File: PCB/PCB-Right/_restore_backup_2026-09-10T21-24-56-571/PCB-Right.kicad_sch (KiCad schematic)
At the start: 56 parts, among them J1 USB_C_Receptacle_USB2.0_16P, J2 Conn_ARM_JTAG_SWD_10, Q1 2N7002, SW1 SW_RST, SW2 SW_SPDT, U2 XC6206PxxxMR, U3 SRV05-4, U4 BQ24075RGT, U5 MDBT50Q-1MV2, Y1 32.768KHz

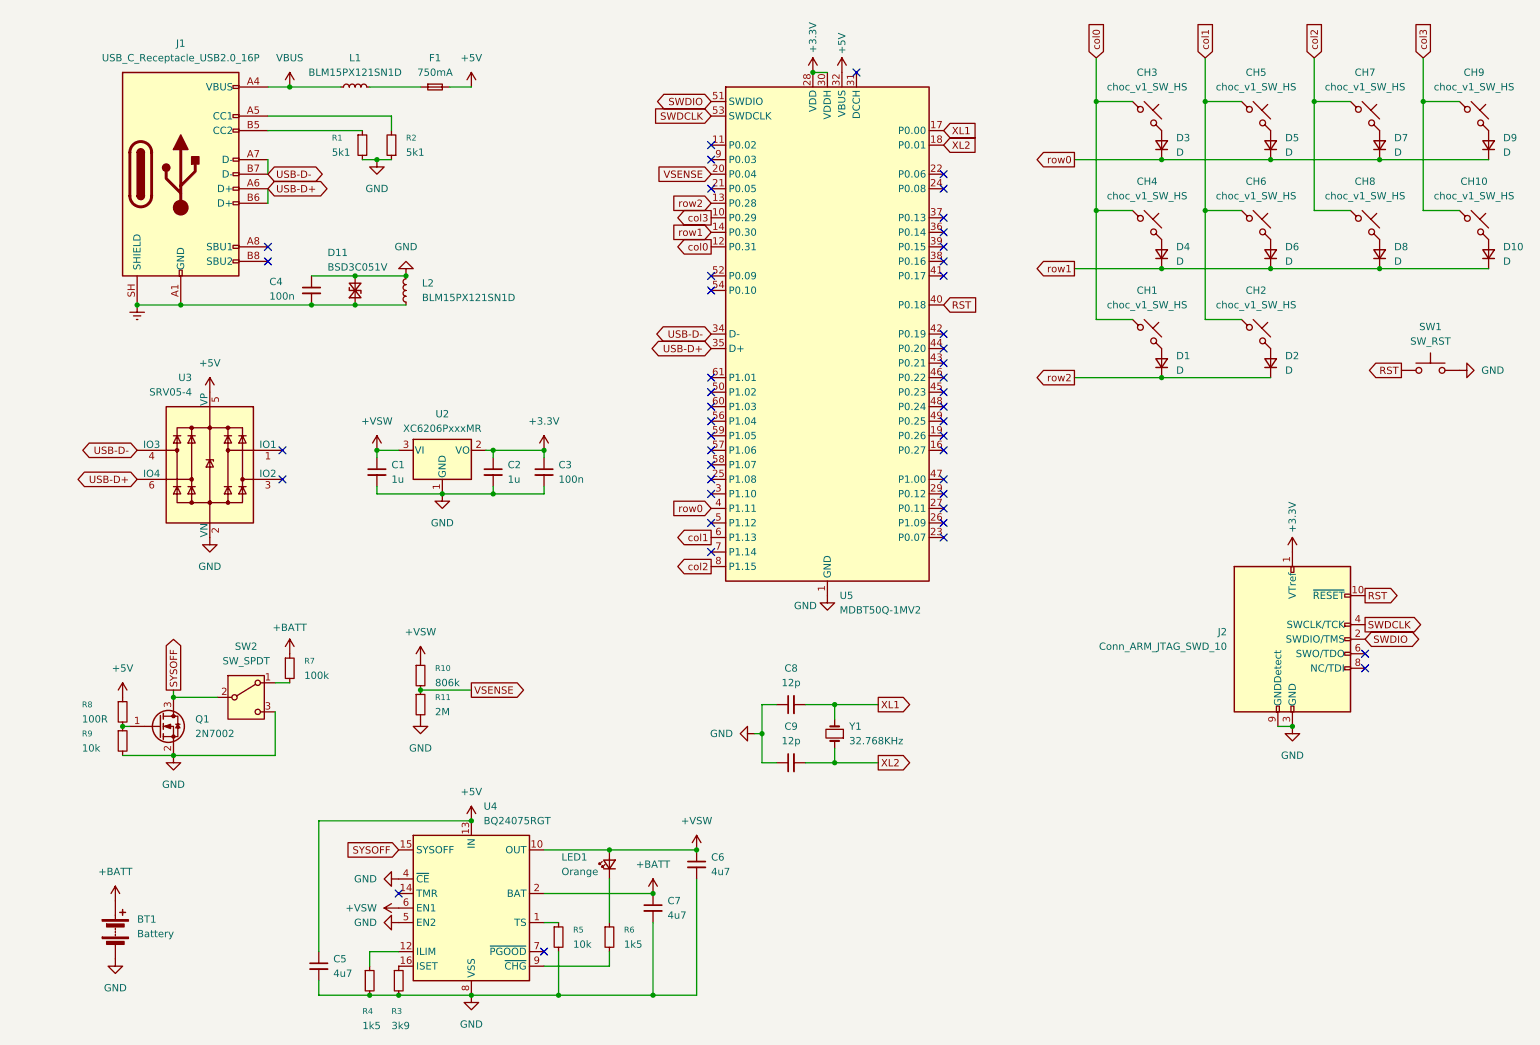
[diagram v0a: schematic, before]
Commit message: PCB Right
Switched to raytac module
gasket mount
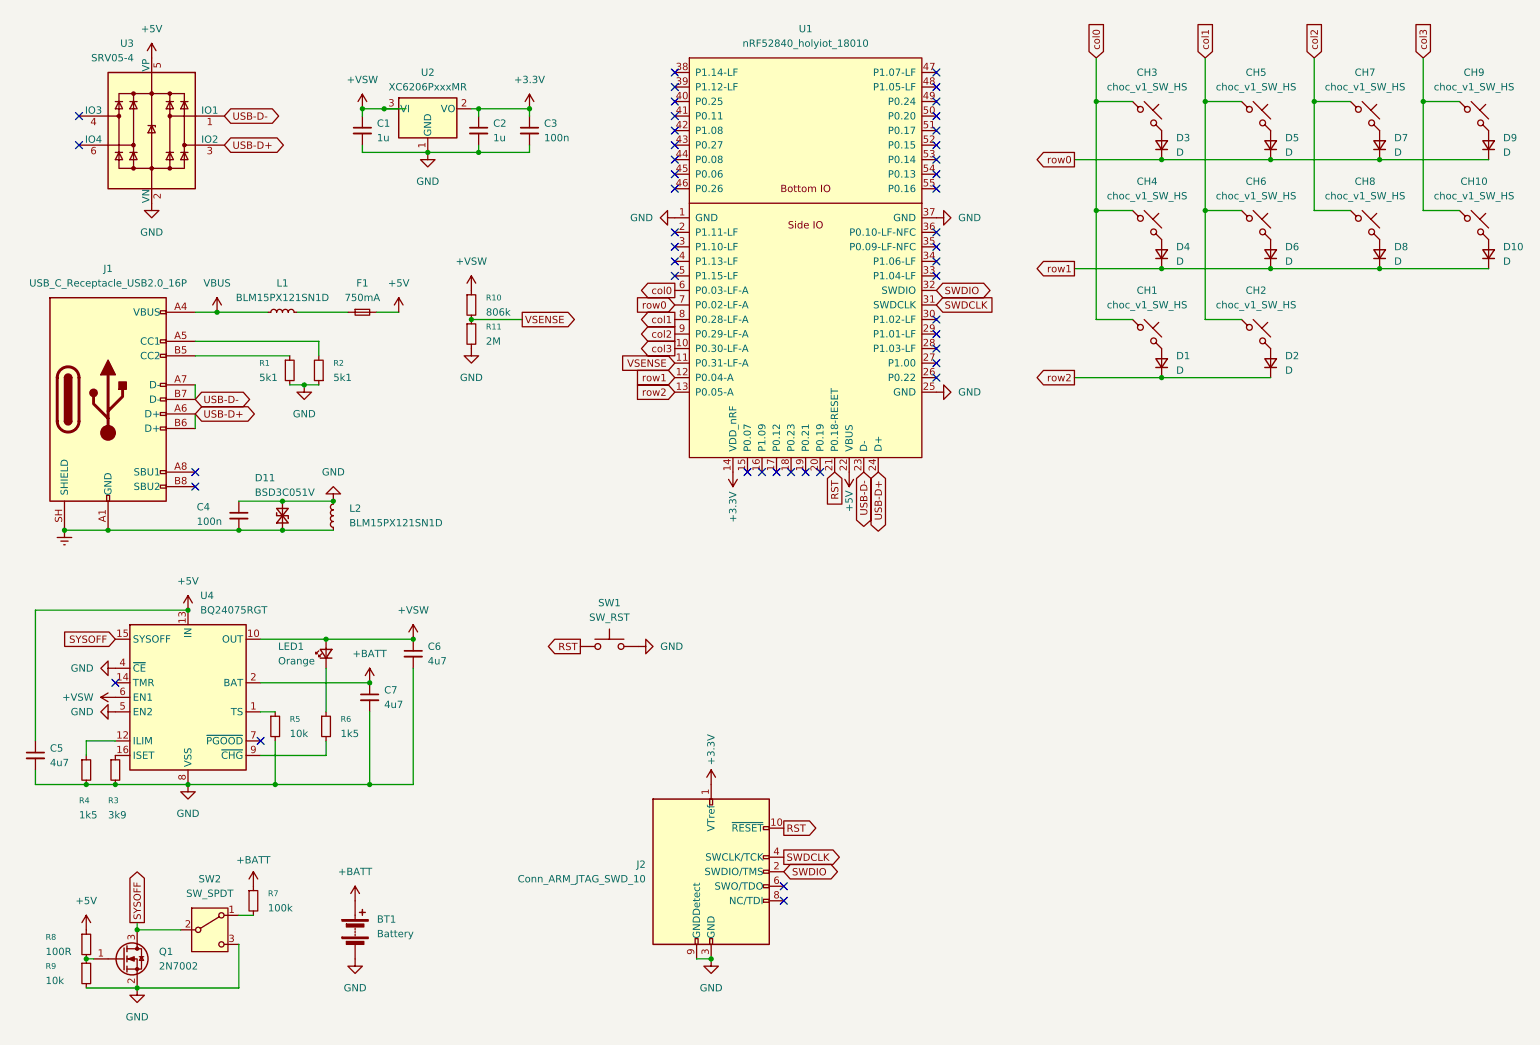
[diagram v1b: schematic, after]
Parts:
- removed C8, C9: 12p, Capacitor_SMD:C_0603_1608Metric, symbol Device:C_Small
- removed U5: MDBT50Q-1MV2, RF_Module:Raytac_MDBT50Q, symbol RF_Module:MDBT50Q-1MV2
- removed Y1: 32.768KHz, Crystal:Crystal_SMD_3215-2Pin_3.2x1.5mm, symbol Device:Crystal_Small
- added U1: nRF52840_holyiot_18010, marbastlib-various:nRF52840_holyiot_18010_HS_simple, symbol marbastlib-various:nRF52840_holyiot_18010
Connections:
- net +3.3V: now also U1.14 (VDD_nRF)
- net +5V: now also U1.22 (VBUS)
- net GND: now also U1.1 (GND), U1.25 (GND), U1.37 (GND)
- net RST: now also U1.21 (P0.18-RESET)
- net SWDCLK: now also U1.31 (SWDCLK)
- net SWDIO: now also U1.32 (SWDIO)
- net USB-D+: now also U3.3 (IO2), U1.24 (D+); no longer U3.6 (IO4)
- net USB-D-: now also U3.1 (IO1), U1.23 (D-); no longer U3.4 (IO3)
- net VSENSE: now also U1.11 (P0.31-LF-A)
- net col0: now also U1.6 (P0.03-LF-A)
- net col1: now also U1.8 (P0.28-LF-A)
- net col2: now also U1.9 (P0.29-LF-A)
- net col3: now also U1.10 (P0.30-LF-A)
- net row0: now also U1.7 (P0.02-LF-A)
- net row1: now also U1.12 (P0.04-A)
- net row2: now also U1.13 (P0.05-A)
- no-connect marks 46 -> 45
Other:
- moved on the sheet: BT1, C1, C2, C3, C4, C5, C6, C7, D11, F1, J1, J2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
